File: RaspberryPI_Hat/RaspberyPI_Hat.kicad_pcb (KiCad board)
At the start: 2 copper layers, 65 x 56 mm, 41 parts, among them Q1 BC817, Q2 BC817, Q3 BC817, SW1 SW_PUSH, U1 CAT24C32WI-GT3

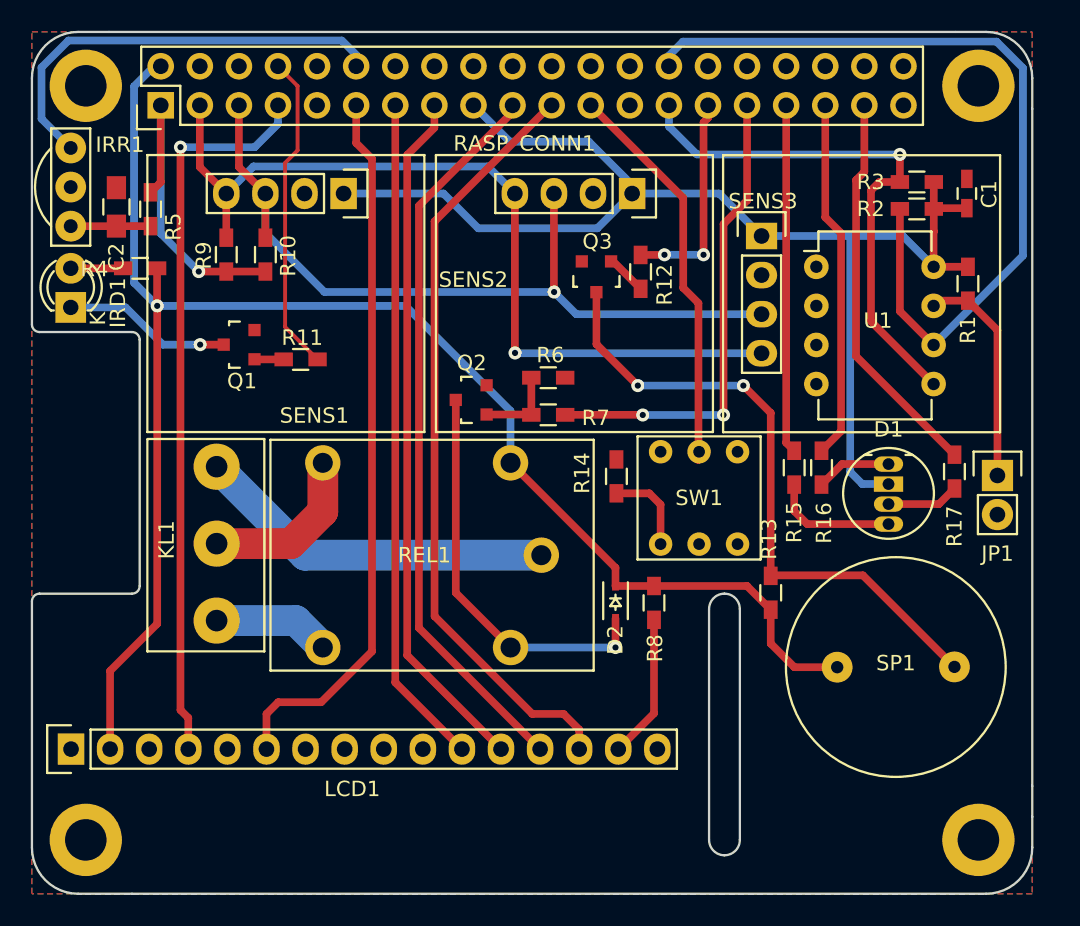
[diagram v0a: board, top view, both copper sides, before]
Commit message: IR Diod moved to pin 11
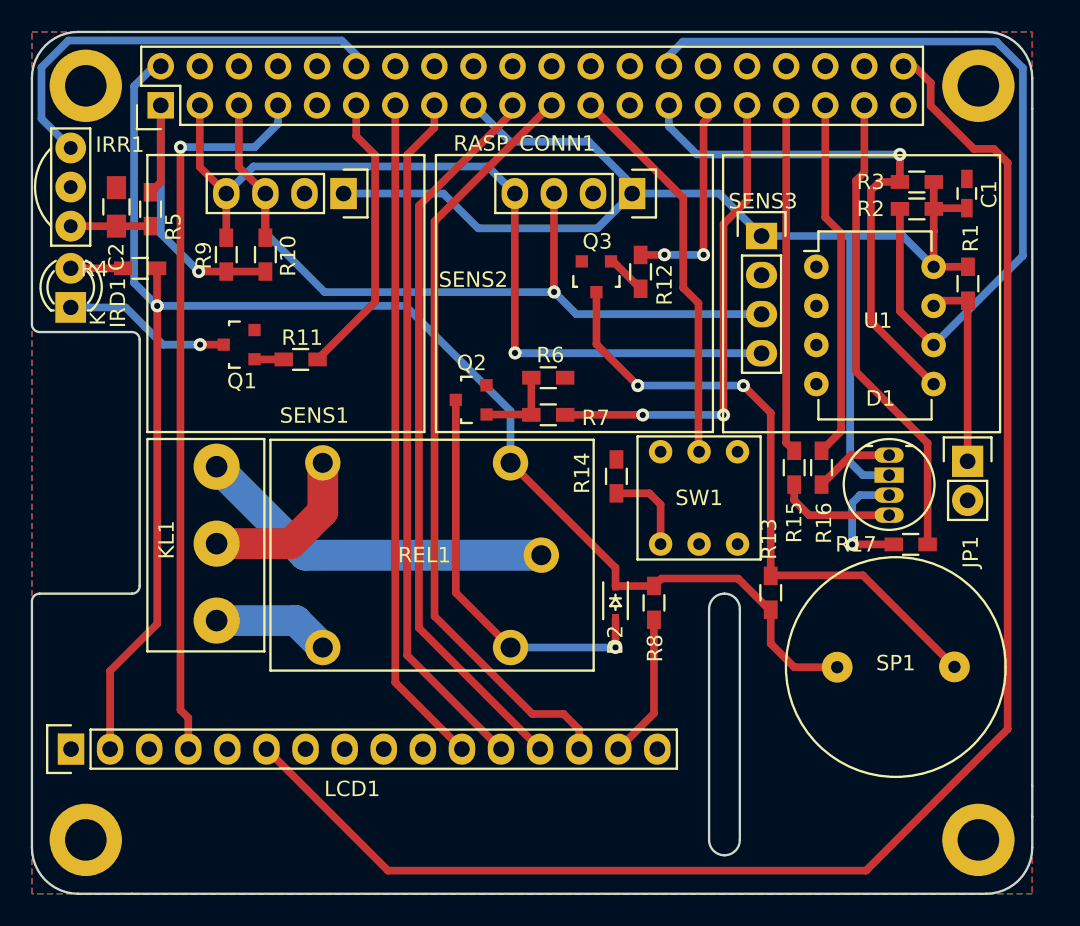
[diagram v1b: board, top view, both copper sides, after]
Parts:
- moved R17 5.52 mm to (155.1, 101.9), turned to 0 degrees
- moved JP1 2.15 mm to (158.8, 96.5)
- moved D1 0.58 mm to (153.7, 96.1)
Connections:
- RASP_CONN1 pad 11: /EN -> Net-(R11-Pad2)
- RASP_CONN1 pad 40: Net-(RASP_CONN1-Pad40) -> /EN
- RASP_CONN1 pad 8: Net-(R11-Pad2) -> Net-(RASP_CONN1-Pad8)
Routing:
- net /EN: track 46.7 -> 102.5 mm
- net /LED3: track 25.6 -> 30.7 mm
- net Net-(D1-Pad3): track 4.70 -> 8.01 mm, vias 0 -> 1
- net Net-(R11-Pad2): track 20.8 -> 18.6 mm
- net Net-(JP1-Pad1): track 14.5 -> 13.1 mm
- net Net-(D1-Pad4): track 8.20 -> 7.59 mm
- net +3V3: track 106.1 -> 105.5 mm

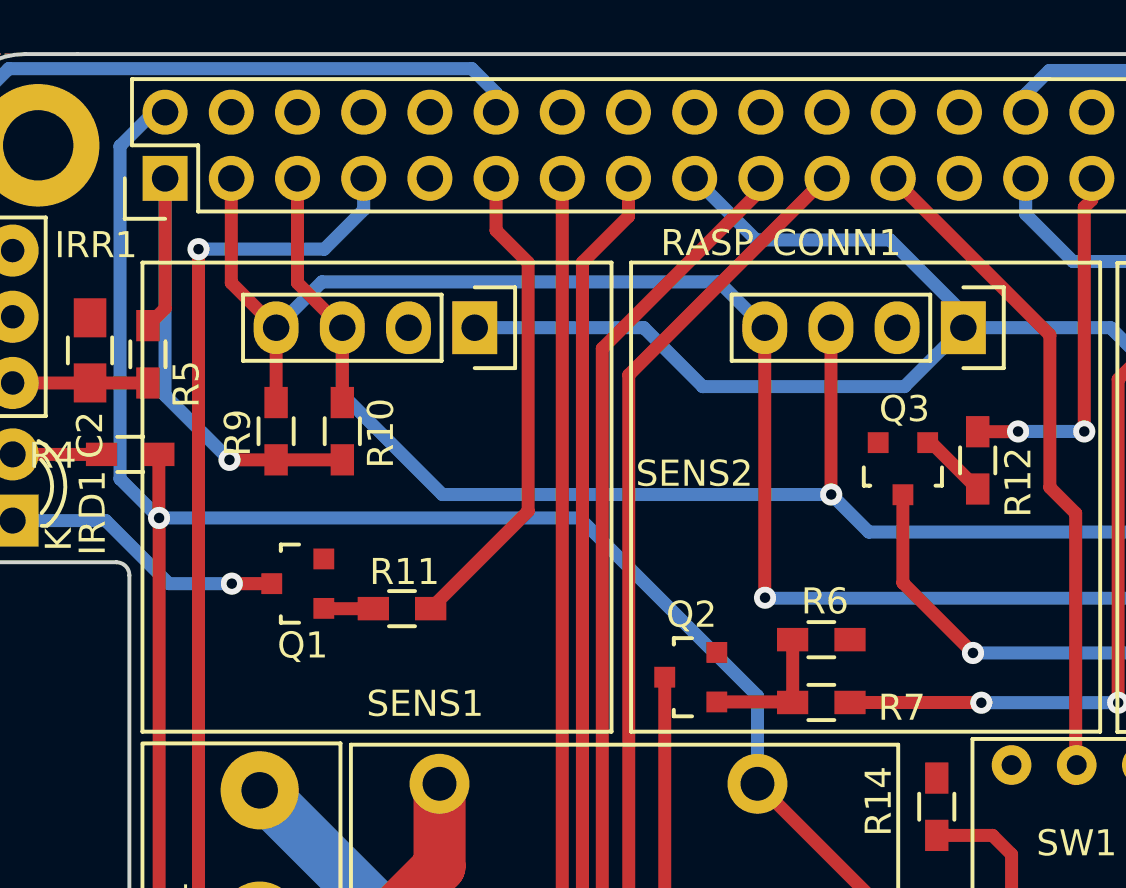
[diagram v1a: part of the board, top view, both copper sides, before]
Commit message: RS interface added
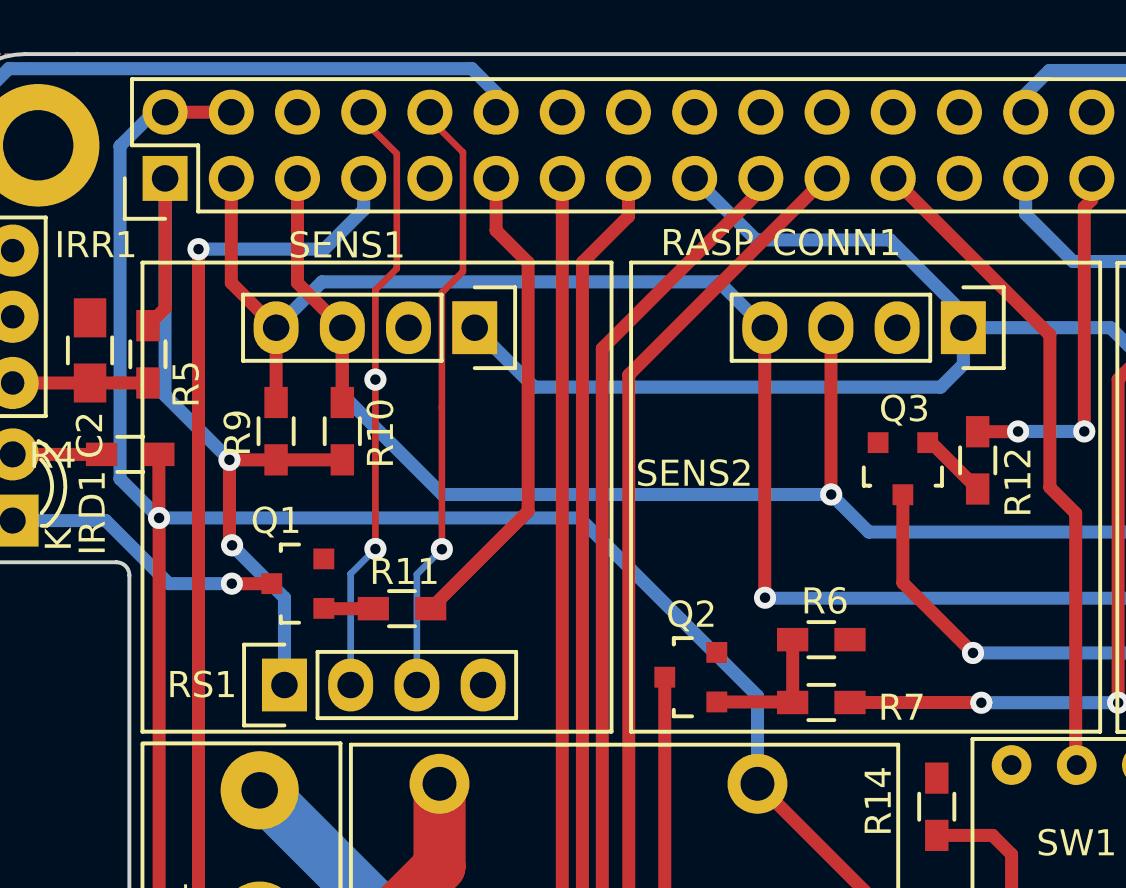
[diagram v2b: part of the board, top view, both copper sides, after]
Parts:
- added RS1: CONN_01X04, Pin_Headers:Pin_Header_Straight_1x04, F.Cu at (111.0, 92.8)
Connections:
- RASP_CONN1 pad 10: Net-(RASP_CONN1-Pad10) -> /RXD
- RASP_CONN1 pad 8: Net-(RASP_CONN1-Pad8) -> /TXD
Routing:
- net /TXD: track 0.00 -> 23.2 mm, vias 0 -> 2
- net /RXD: track 0.00 -> 23.2 mm, vias 0 -> 1
- net +3V3: track 105.5 -> 115.9 mm, vias 1 -> 2
- net +5V: track 108.2 -> 110.8 mm

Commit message: Added logo
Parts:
- added G***: LOGO, myfootprint:LOGO, F.Cu at (122.2, 120.5)

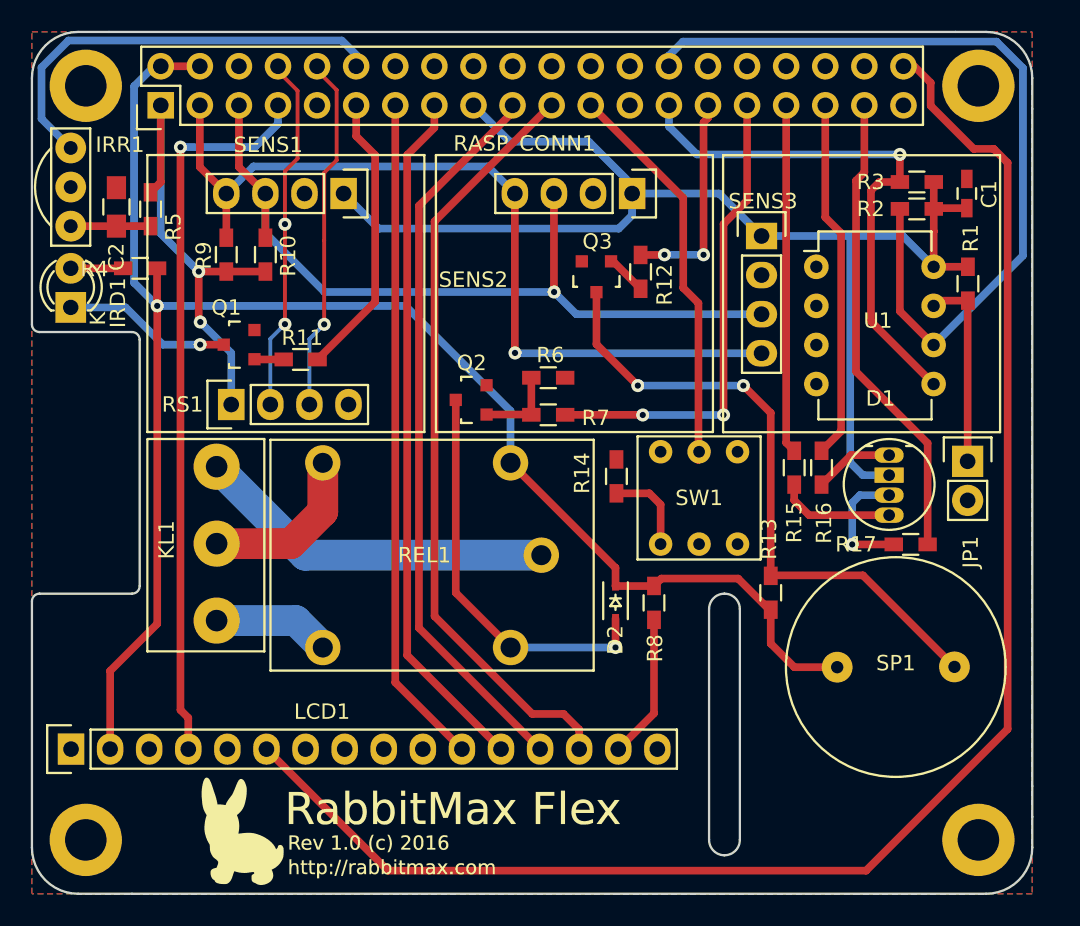
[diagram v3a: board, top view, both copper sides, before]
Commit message: Text on socket's pads
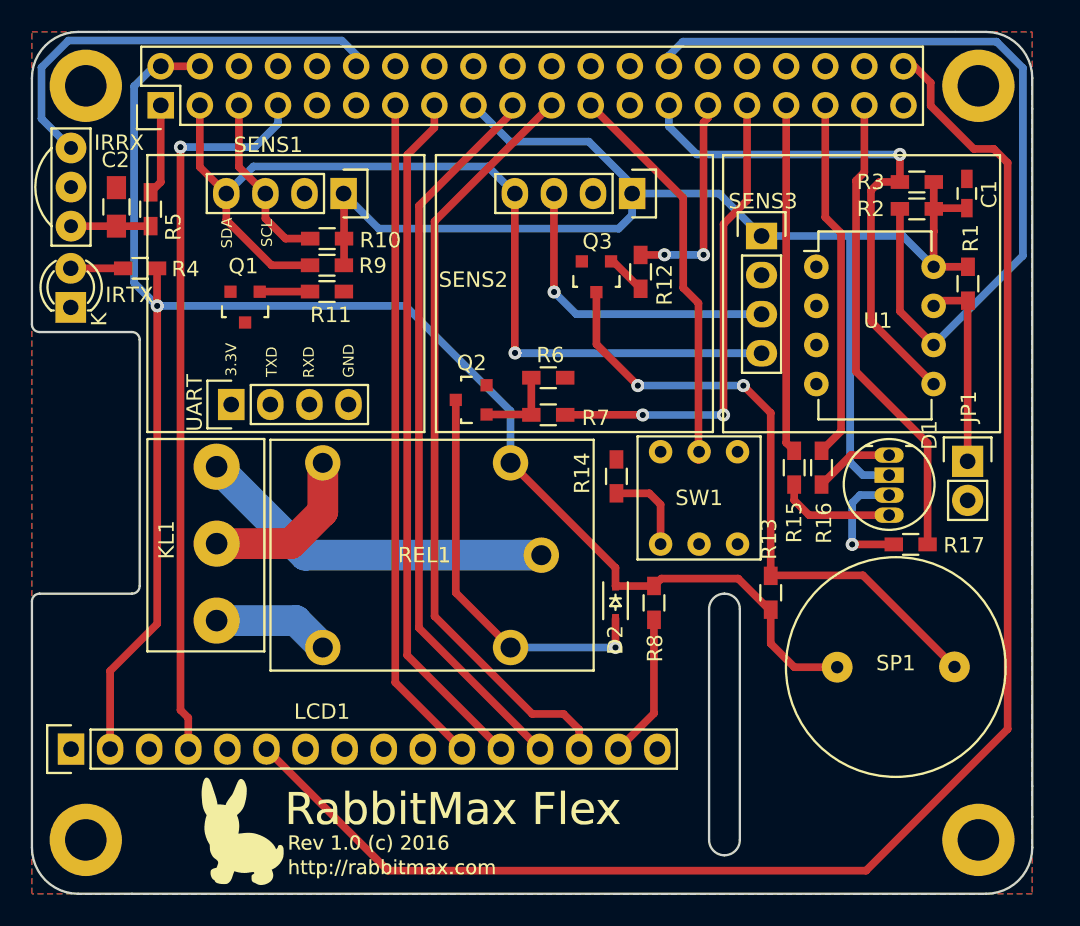
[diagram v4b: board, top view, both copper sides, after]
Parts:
- removed IRD1: L-934F3BT, LEDs:LED-3MM
- removed IRR1: TSOP34838, myfootprint:TSOP38X
- removed RS1: CONN_01X04, Pin_Headers:Pin_Header_Straight_1x04
- added IRRX: TSOP34838, myfootprint:TSOP38X, F.Cu at (103.1, 78.7)
- added IRTX: L-934F3BT, LEDs:LED-3MM, F.Cu at (100.5, 86.5)
- added UART: CONN_01X04, Pin_Headers:Pin_Header_Straight_1x04, F.Cu at (111.0, 92.8)
- moved R9 6.58 mm to (117.2, 83.8), turned to 180 degrees
- moved R11 4.73 mm to (117.2, 85.5)
- moved R10 4.14 mm to (117.2, 82.0), turned to 180 degrees
- moved Q1 2.47 mm to (111.8, 86.5), turned to 180 degrees
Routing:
- net /RXD: track 23.2 -> 0.27 mm, vias 1 -> 0
- net /TXD: track 23.2 -> 0.33 mm, vias 2 -> 0
- net +3V3: track 115.9 -> 94.9 mm, vias 2 -> 0
- net Net-(R10-Pad2): track 52.7 -> 32.0 mm
- net Net-(R11-Pad2): track 18.6 -> 0.00 mm
- net Net-(IRTX1-Pad1): track 10.9 -> 0.00 mm, vias 1 -> 0
- net Net-(R9-Pad2): track 55.9 -> 61.4 mm
- net Net-(Q1-Pad1): track 1.90 -> 3.27 mm
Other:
- board text added: "3.3V"
- board text added: "GND"
- board text added: "RXD"
- board text added: "SCL"
- board text added: "SDA"
- board text added: "TXD"
